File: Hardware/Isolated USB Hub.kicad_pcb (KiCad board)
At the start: 4 copper layers, 100 x 75.3 mm, 80 parts, among them J1 PWR_IN, J2 USB_US, J3 USB_A_Double, J4 USB_A_Double, J5 USB_A_Double, J6 HUB_PROG, U10 USBLC6-2SC6, U11 USBLC6-2SC6, U12 USBLC6-2SC6, U13 USBLC6-2SC6, U14 24LC02BT-I_OT, U15 USBLC6-2SC6, U2 USBLC6-2SC6, U3 LF33_TO252, U4 USB2513B_Bi, U5 NMUSB202MC-R7, U6 NMUSB202MC-R7, U7 NMUSB202MC-R7, U9 USBLC6-2SC6, Y1 Crystal

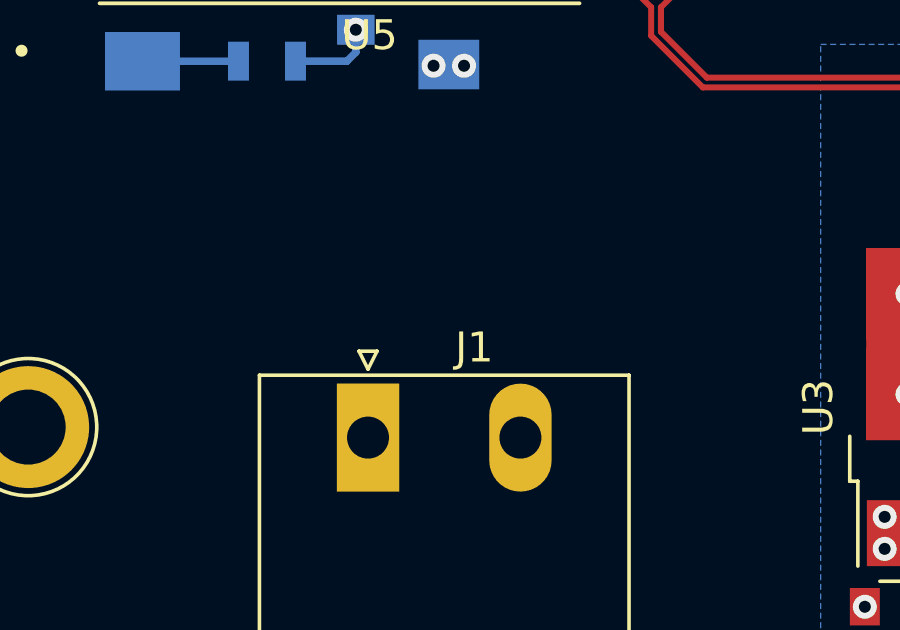
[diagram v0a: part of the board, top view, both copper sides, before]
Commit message: Add power LED
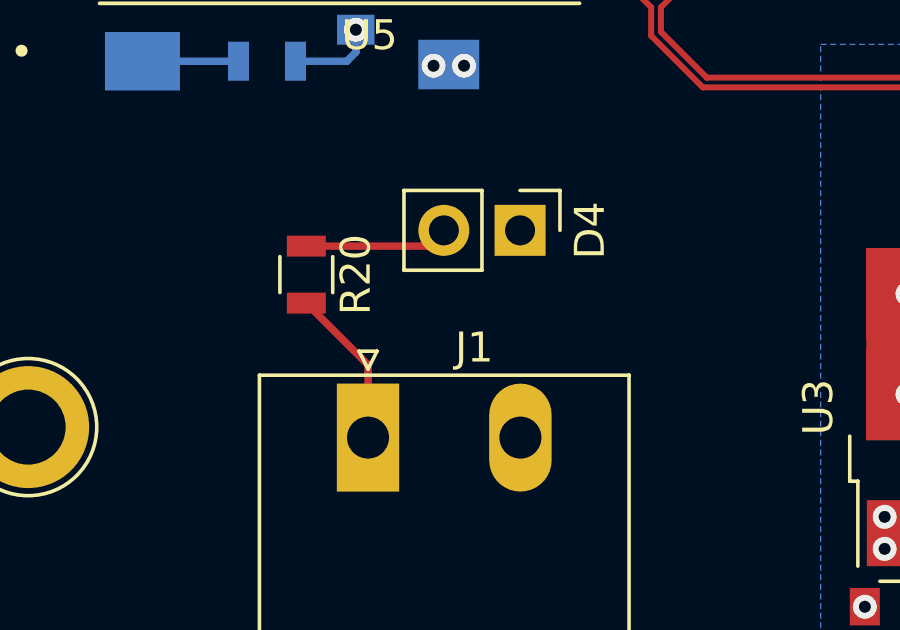
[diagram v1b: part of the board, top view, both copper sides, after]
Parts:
- added D4: PLED, Pin_Headers:Pin_Header_Straight_1x02_Pitch2.54mm, F.Cu at (36.7, 73.8)
- added R20: 470, Resistors_SMD:R_0805, F.Cu at (29.6, 75.2)
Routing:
- net +5V: track 2.37 -> 7.71 mm
- net Net-(D4-Pad2): track 0.00 -> 4.80 mm
